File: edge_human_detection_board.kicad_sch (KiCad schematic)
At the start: 6 parts, among them IC1 TXB0108PWR

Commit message: sc
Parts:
- removed D1, D2, D3: WS2812B, LED_SMD:LED_WS2812B_PLCC4_5.0x5.0mm_P3.2mm, symbol LED:WS2812B
- removed IC1: TXB0108PWR, SOP65P640X120-20N, symbol 00_project_parts:TXB0108PWR
- removed U1: ~, symbol 00_project_parts:coral_micro_board
- removed U2: ~, symbol 00_project_parts:SATEL-VL53L8A
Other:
- added sheet Coral Micro Breakouts (coral_micro_breakout.kicad_sch)
- added sheet RGB Signalling (rgb_signalling.kicad_sch)
- added sheet TOF Sensor (tof_sensorkicad_sch.kicad_sch)
- title: (none) -> EDGE HUMAN DETECTION BOARD

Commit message: made board
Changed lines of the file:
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@@
 	(wire
 		(pts
-			(xy 97.79 71.12) (xy 119.38 71.12)
-		)
-		(stroke
-			(width 0)
-			(type default)
-		)
-	)
-	(wire
-		(pts
-			(xy 97.79 77.47) (xy 119.38 77.47)
-		)
-		(stroke
-			(width 0)
-			(type default)
-		)
-	)
-	(wire
-		(pts
-			(xy 97.79 83.82) (xy 119.38 83.82)
-		)
-		(stroke
-			(width 0)
-			(type default)
-		)
-	)
-	(wire
-		(pts
-			(xy 147.32 68.58) (xy 173.99 68.58)
-		)
-		(stroke
-			(width 0)
-			(type default)
-		)
-	)
-	(wire
-		(pts
-			(xy 147.32 78.74) (xy 173.99 78.74)
-		)
-		(stroke
-			(width 0)
-			(type default)
-		)
-	)
-	(wire
-		(pts
-			(xy 147.32 73.66) (xy 173.99 73.66)
-		)
-		(stroke
-			(width 0)
-			(type default)
-		)
-	)
-	(wire
-		(pts
-			(xy 147.32 88.9) (xy 173.99 88.9)
-		)
-		(stroke
-			(width 0)
-			(type default)
-		)
-	)
-	(wire
-		(pts
-			(xy 147.32 83.82) (xy 173.99 83.82)
+			(xy 88.9 71.12) (xy 119.38 71.12)
+		)
+		(stroke
+			(width 0)
+			(type default)
+		)
+	)
+	(wire
+		(pts
+			(xy 88.9 77.47) (xy 119.38 77.47)
+		)
+		(stroke
+			(width 0)
+			(type default)
+		)
+	)
+	(wire
+		(pts
+			(xy 88.9 83.82) (xy 119.38 83.82)
+		)
+		(stroke
+			(width 0)
+			(type default)
+		)
+	)
+	(wire
+		(pts
+			(xy 147.32 68.58) (xy 180.34 68.58)
+		)
+		(stroke
+			(width 0)
+			(type default)
+		)
+	)
+	(wire
+		(pts
+			(xy 147.32 78.74) (xy 180.34 78.74)
+		)
+		(stroke
+			(width 0)
+			(type default)
+		)
+	)
+	(wire
+		(pts
+			(xy 147.32 73.66) (xy 180.34 73.66)
+		)
+		(stroke
+			(width 0)
+			(type default)
+		)
+	)
+	(wire
+		(pts
+			(xy 147.32 88.9) (xy 180.34 88.9)
+		)
+		(stroke
+			(width 0)
+			(type default)
+		)
+	)
+	(wire
+		(pts
+			(xy 147.32 83.82) (xy 180.34 83.82)
 		)
 		(stroke
@@
 	)
 	(sheet
-		(at 82.55 66.04)
+		(at 73.66 66.04)
 		(size 15.24 24.13)
-		(fields_autoplaced yes)
 		(stroke
 			(width 0.1524)
@@
 		)
 		(property "Sheetname" "RGB Signalling"
-			(at 82.55 65.3284 0)
+			(at 73.66 65.3284 0)
 			(effects
 				(font
@@
 		)
 		(property "Sheetfile" "rgb_signalling.kicad_sch"
-			(at 82.55 90.7546 0)
+			(at 65.024 90.932 0)
 			(effects
 				(font
@@
 		)
 		(pin "+5VDC" input
-			(at 97.79 71.12 0)
+			(at 88.9 71.12 0)
 			(effects
 				(font
@@
 		)
 		(pin "PWM_0" input
-			(at 97.79 77.47 0)
+			(at 88.9 77.47 0)
 			(effects
 				(font
@@
 		)
 		(pin "+1.8VDC" input
-			(at 97.79 83.82 0)
+			(at 88.9 83.82 0)
 			(effects
 				(font
@@
 	)
 	(sheet
-		(at 173.99 66.04)
+		(at 180.34 66.04)
 		(size 16.51 25.4)
 		(fields_autoplaced yes)
@@
 		)
 		(property "Sheetname" "TOF Sensor"
-			(at 173.99 65.3284 0)
+			(at 180.34 65.3284 0)
 			(effects
 				(font
@@
 		)
 		(property "Sheetfile" "tof_sensorkicad_sch.kicad_sch"
-			(at 173.99 92.0246 0)
+			(at 180.34 92.0246 0)
 			(effects
 				(font
@@
 		)
 		(pin "PWM_1" input
-			(at 173.99 88.9 180)
+			(at 180.34 88.9 180)
 			(effects
 				(font
@@
 		)
 		(pin "+1.8VDC" input
-			(at 173.99 73.66 180)
+			(at 180.34 73.66 180)
 			(effects
 				(font
@@
 		)
 		(pin "SDA" input
-			(at 173.99 83.82 180)
+			(at 180.34 83.82 180)
 			(effects
 				(font
@@
 		)
 		(pin "+3.3VDC" input
-			(at 173.99 68.58 180)
+			(at 180.34 68.58 180)
 			(effects
 				(font
@@
 		)
 		(pin "SCL" input
-			(at 173.99 78.74 180)
-			(effects
-				(font
+			(at 180.34 78.74 180)
+			(effects
+				(font

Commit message: Fab v
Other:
- added sheet usbc_fuse (usbc_fuse.kicad_sch)
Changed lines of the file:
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@@
+		)
+	)
+	(sheet
+		(at 121.92 113.03)
+		(size 22.86 15.24)
+		(fields_autoplaced yes)
+		(stroke
+			(width 0.1524)
+			(type solid)
+		)
+		(fill
+			(color 0 0 0 0.0000)
+		)
+		(property "Sheetname" "usbc_fuse"
+			(at 121.92 112.3184 0)
+			(effects
+				(font
+					(size 1.27 1.27)
+				)
+				(justify left bottom)
+			)
+		)
+		(property "Sheetfile" "usbc_fuse.kicad_sch"
+			(at 121.92 128.8546 0)
+			(effects
+				(font
+					(size 1.27 1.27)
+				)
+				(justify left top)
+			)
+		)
+		(instances
+			(project "edge_human_detection_board"
+				(path "/f7edb1cc-a42a-4cc0-9a6f-d9bd2b944353"
+					(page "5")
+				)
+			)
 		)
 	)

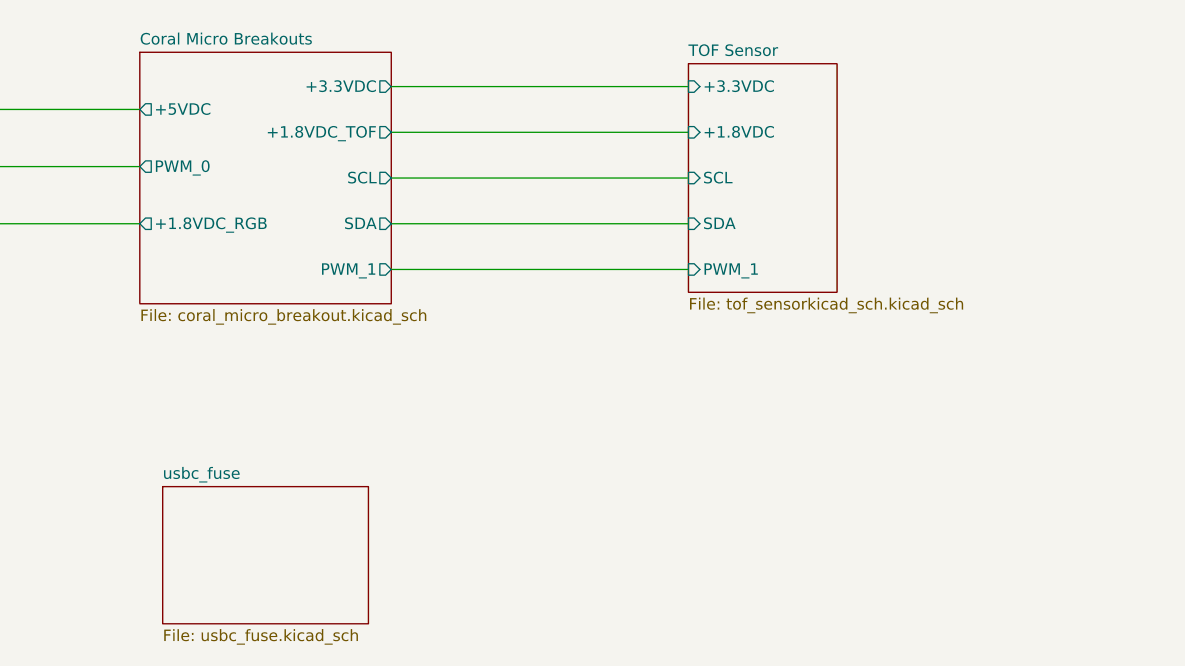
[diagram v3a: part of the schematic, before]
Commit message: not working, reverting to old design
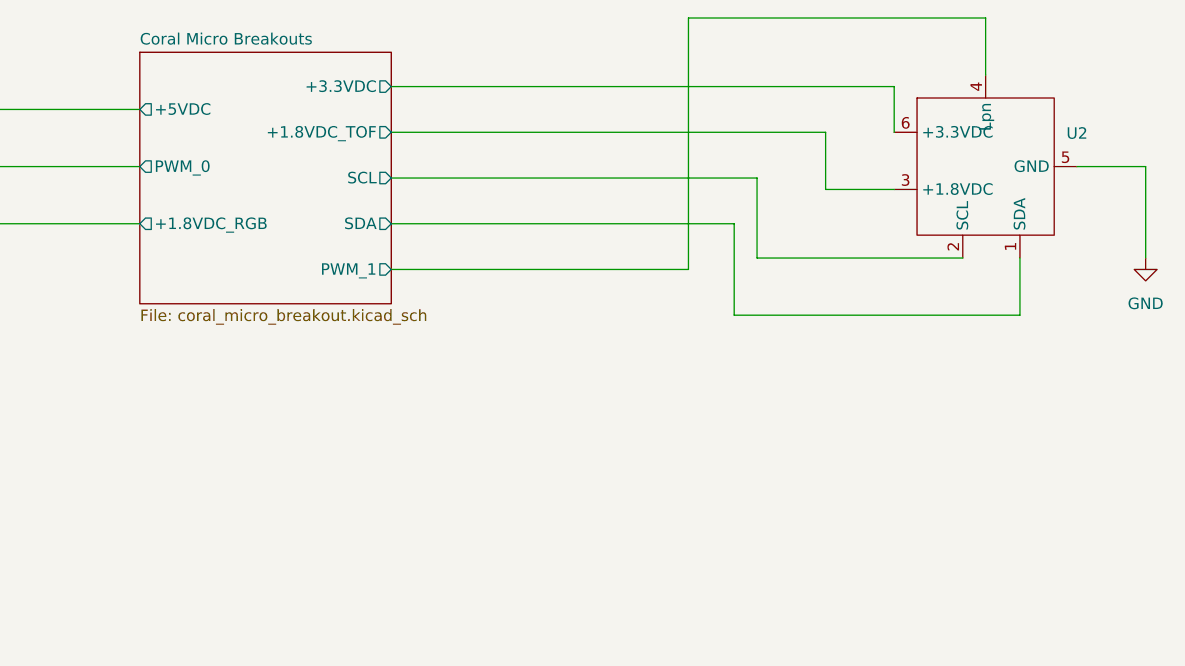
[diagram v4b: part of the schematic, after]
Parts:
- added U2: ~, 00_parts_lib:TOF_MODULE, symbol 00_project_parts:tof_module
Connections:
- net Coral Micro Breakouts/+1.8VDC_TOF: now also U2.3 (+1.8VDC)
- net Coral Micro Breakouts/+3.3VDC: now also U2.6 (+3.3VDC)
- net Coral Micro Breakouts/PWM_1: now also U2.4 (Lpn)
- net Coral Micro Breakouts/SCL: now also U2.2 (SCL)
- net Coral Micro Breakouts/SDA: now also U2.1 (SDA)
- new net GND: U2.5 (GND)
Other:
- removed sheet TOF Sensor
- removed sheet usbc_fuse
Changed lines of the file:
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@@
+	(wire
+		(pts
+			(xy 203.2 73.66) (xy 203.2 68.58)
+		)
+		(stroke
+			(width 0)
+			(type default)
+		)
+	)
+	(wire
+		(pts
+			(xy 223.52 77.47) (xy 231.14 77.47)
+		)
+		(stroke
+			(width 0)
+			(type default)
+		)
+	)
+	(wire
+		(pts
+			(xy 195.58 73.66) (xy 195.58 80.01)
+		)
+		(stroke
+			(width 0)
+			(type default)
+		)
+	)
+	(wire
+		(pts
+			(xy 180.34 60.96) (xy 213.36 60.96)
+		)
+		(stroke
+			(width 0)
+			(type default)
+		)
+	)
 	(wire
 		(pts
@@
 	(wire
 		(pts
+			(xy 231.14 77.47) (xy 231.14 87.63)
+		)
+		(stroke
+			(width 0)
+			(type default)
+		)
+	)
+	(wire
+		(pts
 			(xy 88.9 83.82) (xy 119.38 83.82)
 		)
@@
 	(wire
 		(pts
-			(xy 147.32 68.58) (xy 180.34 68.58)
-		)
-		(stroke
-			(width 0)
-			(type default)
-		)
-	)
-	(wire
-		(pts
-			(xy 147.32 78.74) (xy 180.34 78.74)
-		)
-		(stroke
-			(width 0)
-			(type default)
-		)
-	)
-	(wire
-		(pts
-			(xy 147.32 73.66) (xy 180.34 73.66)
+			(xy 147.32 68.58) (xy 203.2 68.58)
+		)
+		(stroke
+			(width 0)
+			(type default)
+		)
+	)
+	(wire
+		(pts
+			(xy 147.32 78.74) (xy 187.96 78.74)
+		)
+		(stroke
+			(width 0)
+			(type default)
+		)
+	)
+	(wire
+		(pts
+			(xy 187.96 78.74) (xy 187.96 87.63)
+		)
+		(stroke
+			(width 0)
+			(type default)
+		)
+	)
+	(wire
+		(pts
+			(xy 195.58 80.01) (xy 203.2 80.01)
+		)
+		(stroke
+			(width 0)
+			(type default)
+		)
+	)
+	(wire
+		(pts
+			(xy 147.32 73.66) (xy 195.58 73.66)
 		)
 		(stroke
@@
 	(wire
 		(pts
-			(xy 147.32 83.82) (xy 180.34 83.82)
-		)
-		(stroke
-			(width 0)
-			(type default)
+			(xy 187.96 87.63) (xy 210.82 87.63)
+		)
+		(stroke
+			(width 0)
+			(type default)
+		)
+	)
+	(wire
+		(pts
+			(xy 217.17 93.98) (xy 217.17 87.63)
+		)
+		(stroke
+			(width 0)
+			(type default)
+		)
+	)
+	(wire
+		(pts
+			(xy 213.36 60.96) (xy 213.36 67.31)
+		)
+		(stroke
+			(width 0)
+			(type default)
+		)
+	)
+	(wire
+		(pts
+			(xy 185.42 83.82) (xy 185.42 93.98)
+		)
+		(stroke
+			(width 0)
+			(type default)
+		)
+	)
+	(wire
+		(pts
+			(xy 185.42 93.98) (xy 217.17 93.98)
+		)
+		(stroke
+			(width 0)
+			(type default)
+		)
+	)
+	(wire
+		(pts
+			(xy 180.34 88.9) (xy 180.34 60.96)
+		)
+		(stroke
+			(width 0)
+			(type default)
+		)
+	)
+	(wire
+		(pts
+			(xy 147.32 83.82) (xy 185.42 83.82)
+		)
+		(stroke
+			(width 0)
+			(type default)
+		)
+	)
+	(symbol
+		(lib_id "00_project_parts:tof_module")
+		(at 213.36 77.47 0)
+		(unit 1)
+		(exclude_from_sim no)
+		(in_bom yes)
+		(on_board yes)
+		(dnp no)
+		(fields_autoplaced yes)
+		(property "Reference" "U2"
+			(at 223.52 73.7868 0)
+			(effects
+				(font
+					(size 1.27 1.27)
+				)
+			)
+		)
+		(property "Value" "~"
+			(at 223.52 75.6919 0)
+			(effects
+				(font
+					(size 1.27 1.27)
+				)
+			)
+		)
+		(property "Footprint" "00_parts_lib:TOF_MODULE"
+			(at 213.36 77.47 0)
+			(effects
+				(font
+					(size 1.27 1.27)
+				)
+				(hide yes)
+			)
+		)
+		(property "Datasheet" ""
+			(at 213.36 77.47 0)
+			(effects
+				(font
+					(size 1.27 1.27)
+				)
+				(hide yes)
+			)
+		)
+		(property "Description" ""
+			(at 213.36 77.47 0)
+			(effects
+				(font
+					(size 1.27 1.27)
+				)
+				(hide yes)
+			)
+		)
+		(pin "4"
+		)
+		(pin "1"
+		)
+		(pin "2"
+		)
+		(pin "5"
+		)
+		(pin "3"
+		)
+		(pin "6"
+		)
+		(instances
+			(project ""
+				(path "/f7edb1cc-a42a-4cc0-9a6f-d9bd2b944353"
+					(reference "U2")
+					(unit 1)
+				)
+			)
+		)
+	)
+	(symbol
+		(lib_id "power:GND")
+		(at 231.14 87.63 0)
+		(unit 1)
+		(exclude_from_sim no)
+		(in_bom yes)
+		(on_board yes)
+		(dnp no)
+		(fields_autoplaced yes)
+		(property "Reference" "#PWR017"
+			(at 231.14 93.98 0)
+			(effects
+				(font
+					(size 1.27 1.27)
+				)
+				(hide yes)
+			)
+		)
+		(property "Value" "GND"
+			(at 231.14 92.71 0)
+			(effects
+				(font
+					(size 1.27 1.27)
+				)
+			)
+		)
+		(property "Footprint" ""
+			(at 231.14 87.63 0)
+			(effects
+				(font
+					(size 1.27 1.27)
+				)
+				(hide yes)
+			)
+		)
+		(property "Datasheet" ""
+			(at 231.14 87.63 0)
+			(effects
+				(font
+					(size 1.27 1.27)
+				)
+				(hide yes)
+			)
+		)
+		(property "Description" "Power symbol creates a global label with name \"GND\" , ground"
+			(at 231.14 87.63 0)
+			(effects
+				(font
+					(size 1.27 1.27)
+				)
+				(hide yes)
+			)
+		)
+		(pin "1"
+		)
+		(instances
+			(project ""
+				(path "/f7edb1cc-a42a-4cc0-9a6f-d9bd2b944353"
+					(reference "#PWR017")
+					(unit 1)
+				)
+			)
 		)
 	)
@@
 				)
 			)
-		)
-	)
-	(sheet
-		(at 180.34 66.04)
-		(size 16.51 25.4)
-		(fields_autoplaced yes)
-		(stroke
-			(width 0.1524)
-			(type solid)
-		)
-		(fill
-			(color 0 0 0 0.0000)
-		)
-		(property "Sheetname" "TOF Sensor"
-			(at 180.34 65.3284 0)
-			(effects
-				(font
-					(size 1.27 1.27)
-				)
-				(justify left bottom)
-			)
-		)
-		(property "Sheetfile" "tof_sensorkicad_sch.kicad_sch"
-			(at 180.34 92.0246 0)
-			(effects
-				(font
-					(size 1.27 1.27)
-				)
-				(justify left top)
-			)
-		)
-		(pin "PWM_1" input
-			(at 180.34 88.9 180)
-			(effects
-				(font
-					(size 1.27 1.27)
-				)
-				(justify left)
-			)
-		)
-		(pin "+1.8VDC" input
-			(at 180.34 73.66 180)
-			(effects
-				(font
-					(size 1.27 1.27)
-				)
-				(justify left)
-			)
-		)
-		(pin "SDA" input
-			(at 180.34 83.82 180)
-			(effects
-				(font
-					(size 1.27 1.27)
-				)
-				(justify left)
-			)
-		)
-		(pin "+3.3VDC" input
-			(at 180.34 68.58 180)
-			(effects
-				(font
-					(size 1.27 1.27)
-				)
-				(justify left)
-			)
-		)
-		(pin "SCL" input
-			(at 180.34 78.74 180)
-			(effects
-				(font
-					(size 1.27 1.27)
-				)
-				(justify left)
-			)
-		)
-		(instances
-			(project "edge_human_detection_board"
-				(path "/f7edb1cc-a42a-4cc0-9a6f-d9bd2b944353"
-					(page "4")
-				)
-			)
-		)
-	)
-	(sheet
-		(at 121.92 113.03)
-		(size 22.86 15.24)
-		(fields_autoplaced yes)
-		(stroke
-			(width 0.1524)
-			(type solid)
-		)
-		(fill
-			(color 0 0 0 0.0000)
-		)
-		(property "Sheetname" "usbc_fuse"
-			(at 121.92 112.3184 0)
-			(effects
-				(font
-					(size 1.27 1.27)
-				)
-				(justify left bottom)
-			)
-		)
-		(property "Sheetfile" "usbc_fuse.kicad_sch"
-			(at 121.92 128.8546 0)
-			(effects
-				(font
-					(size 1.27 1.27)
-				)
-				(justify left top)
-			)
-		)
-		(instances
-			(project "edge_human_detection_board"
-				(path "/f7edb1cc-a42a-4cc0-9a6f-d9bd2b944353"
-					(page "5")
-				)
-			)

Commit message: latest updates, up to v2
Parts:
- removed U2: ~, 00_parts_lib:TOF_MODULE, symbol 00_project_parts:tof_module
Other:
- added sheet TOF Sensor (tof_sensorkicad_sch.kicad_sch)
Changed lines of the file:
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@@
-	(wire
-		(pts
-			(xy 203.2 73.66) (xy 203.2 68.58)
-		)
-		(stroke
-			(width 0)
-			(type default)
-		)
-	)
-	(wire
-		(pts
-			(xy 223.52 77.47) (xy 231.14 77.47)
-		)
-		(stroke
-			(width 0)
-			(type default)
-		)
-	)
-	(wire
-		(pts
-			(xy 195.58 73.66) (xy 195.58 80.01)
-		)
-		(stroke
-			(width 0)
-			(type default)
-		)
-	)
-	(wire
-		(pts
-			(xy 180.34 60.96) (xy 213.36 60.96)
-		)
-		(stroke
-			(width 0)
-			(type default)
-		)
-	)
 	(wire
 		(pts
@@
 	(wire
 		(pts
-			(xy 231.14 77.47) (xy 231.14 87.63)
-		)
-		(stroke
-			(width 0)
-			(type default)
-		)
-	)
-	(wire
-		(pts
 			(xy 88.9 83.82) (xy 119.38 83.82)
 		)
@@
 	(wire
 		(pts
-			(xy 147.32 68.58) (xy 203.2 68.58)
-		)
-		(stroke
-			(width 0)
-			(type default)
-		)
-	)
-	(wire
-		(pts
-			(xy 147.32 78.74) (xy 187.96 78.74)
-		)
-		(stroke
-			(width 0)
-			(type default)
-		)
-	)
-	(wire
-		(pts
-			(xy 187.96 78.74) (xy 187.96 87.63)
-		)
-		(stroke
-			(width 0)
-			(type default)
-		)
-	)
-	(wire
-		(pts
-			(xy 195.58 80.01) (xy 203.2 80.01)
-		)
-		(stroke
-			(width 0)
-			(type default)
-		)
-	)
-	(wire
-		(pts
-			(xy 147.32 73.66) (xy 195.58 73.66)
+			(xy 147.32 68.58) (xy 180.34 68.58)
+		)
+		(stroke
+			(width 0)
+			(type default)
+		)
+	)
+	(wire
+		(pts
+			(xy 147.32 78.74) (xy 180.34 78.74)
+		)
+		(stroke
+			(width 0)
+			(type default)
+		)
+	)
+	(wire
+		(pts
+			(xy 147.32 73.66) (xy 180.34 73.66)
 		)
 		(stroke
@@
 	(wire
 		(pts
-			(xy 187.96 87.63) (xy 210.82 87.63)
-		)
-		(stroke
-			(width 0)
-			(type default)
-		)
-	)
-	(wire
-		(pts
-			(xy 217.17 93.98) (xy 217.17 87.63)
-		)
-		(stroke
-			(width 0)
-			(type default)
-		)
-	)
-	(wire
-		(pts
-			(xy 213.36 60.96) (xy 213.36 67.31)
-		)
-		(stroke
-			(width 0)
-			(type default)
-		)
-	)
-	(wire
-		(pts
-			(xy 185.42 83.82) (xy 185.42 93.98)
-		)
-		(stroke
-			(width 0)
-			(type default)
-		)
-	)
-	(wire
-		(pts
-			(xy 185.42 93.98) (xy 217.17 93.98)
-		)
-		(stroke
-			(width 0)
-			(type default)
-		)
-	)
-	(wire
-		(pts
-			(xy 180.34 88.9) (xy 180.34 60.96)
-		)
-		(stroke
-			(width 0)
-			(type default)
-		)
-	)
-	(wire
-		(pts
-			(xy 147.32 83.82) (xy 185.42 83.82)
-		)
-		(stroke
-			(width 0)
-			(type default)
-		)
-	)
-	(symbol
-		(lib_id "00_project_parts:tof_module")
-		(at 213.36 77.47 0)
-		(unit 1)
-		(exclude_from_sim no)
-		(in_bom yes)
-		(on_board yes)
-		(dnp no)
-		(fields_autoplaced yes)
-		(property "Reference" "U2"
-			(at 223.52 73.7868 0)
-			(effects
-				(font
-					(size 1.27 1.27)
-				)
-			)
-		)
-		(property "Value" "~"
-			(at 223.52 75.6919 0)
-			(effects
-				(font
-					(size 1.27 1.27)
-				)
-			)
-		)
-		(property "Footprint" "00_parts_lib:TOF_MODULE"
-			(at 213.36 77.47 0)
-			(effects
-				(font
-					(size 1.27 1.27)
-				)
-				(hide yes)
-			)
-		)
-		(property "Datasheet" ""
-			(at 213.36 77.47 0)
-			(effects
-				(font
-					(size 1.27 1.27)
-				)
-				(hide yes)
-			)
-		)
-		(property "Description" ""
-			(at 213.36 77.47 0)
-			(effects
-				(font
-					(size 1.27 1.27)
-				)
-				(hide yes)
-			)
-		)
-		(pin "4"
-		)
-		(pin "1"
-		)
-		(pin "2"
-		)
-		(pin "5"
-		)
-		(pin "3"
-		)
-		(pin "6"
-		)
-		(instances
-			(project ""
-				(path "/f7edb1cc-a42a-4cc0-9a6f-d9bd2b944353"
-					(reference "U2")
-					(unit 1)
-				)
-			)
-		)
-	)
-	(symbol
-		(lib_id "power:GND")
-		(at 231.14 87.63 0)
-		(unit 1)
-		(exclude_from_sim no)
-		(in_bom yes)
-		(on_board yes)
-		(dnp no)
-		(fields_autoplaced yes)
-		(property "Reference" "#PWR017"
-			(at 231.14 93.98 0)
-			(effects
-				(font
-					(size 1.27 1.27)
-				)
-				(hide yes)
-			)
-		)
-		(property "Value" "GND"
-			(at 231.14 92.71 0)
-			(effects
-				(font
-					(size 1.27 1.27)
-				)
-			)
-		)
-		(property "Footprint" ""
-			(at 231.14 87.63 0)
-			(effects
-				(font
-					(size 1.27 1.27)
-				)
-				(hide yes)
-			)
-		)
-		(property "Datasheet" ""
-			(at 231.14 87.63 0)
-			(effects
-				(font
-					(size 1.27 1.27)
-				)
-				(hide yes)
-			)
-		)
-		(property "Description" "Power symbol creates a global label with name \"GND\" , ground"
-			(at 231.14 87.63 0)
-			(effects
-				(font
-					(size 1.27 1.27)
-				)
-				(hide yes)
-			)
-		)
-		(pin "1"
-		)
-		(instances
-			(project ""
-				(path "/f7edb1cc-a42a-4cc0-9a6f-d9bd2b944353"
-					(reference "#PWR017")
-					(unit 1)
-				)
-			)
+			(xy 147.32 83.82) (xy 180.34 83.82)
+		)
+		(stroke
+			(width 0)
+			(type default)
 		)
 	)
@@
 				)
 			)
+		)
+	)
+	(sheet
+		(at 180.34 66.04)
+		(size 16.51 25.4)
+		(fields_autoplaced yes)
+		(stroke
+			(width 0.1524)
+			(type solid)
+		)
+		(fill
+			(color 0 0 0 0.0000)
+		)
+		(property "Sheetname" "TOF Sensor"
+			(at 180.34 65.3284 0)
+			(effects
+				(font
+					(size 1.27 1.27)
+				)
+				(justify left bottom)
+			)
+		)
+		(property "Sheetfile" "tof_sensorkicad_sch.kicad_sch"
+			(at 180.34 92.0246 0)
+			(effects
+				(font
+					(size 1.27 1.27)
+				)
+				(justify left top)
+			)
+		)
+		(pin "PWM_1" input
+			(at 180.34 88.9 180)
+			(effects
+				(font
+					(size 1.27 1.27)
+				)
+				(justify left)
+			)
+		)
+		(pin "+1.8VDC" input
+			(at 180.34 73.66 180)
+			(effects
+				(font
+					(size 1.27 1.27)
+				)
+				(justify left)
+			)
+		)
+		(pin "SDA" input
+			(at 180.34 83.82 180)
+			(effects
+				(font
+					(size 1.27 1.27)
+				)
+				(justify left)
+			)
+		)
+		(pin "+3.3VDC" input
+			(at 180.34 68.58 180)
+			(effects
+				(font
+					(size 1.27 1.27)
+				)
+				(justify left)
+			)
+		)
+		(pin "SCL" input
+			(at 180.34 78.74 180)
+			(effects
+				(font
+					(size 1.27 1.27)
+				)
+				(justify left)
+			)
+		)
+		(instances
+			(project "edge_human_detection_board"
+				(path "/f7edb1cc-a42a-4cc0-9a6f-d9bd2b944353"
+					(page "4")
+				)
+			)
